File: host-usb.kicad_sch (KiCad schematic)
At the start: 15 parts, among them J3 USB4105-GF-A-060, U2 USBLC6-2SC6, U5 AP62301WU-7

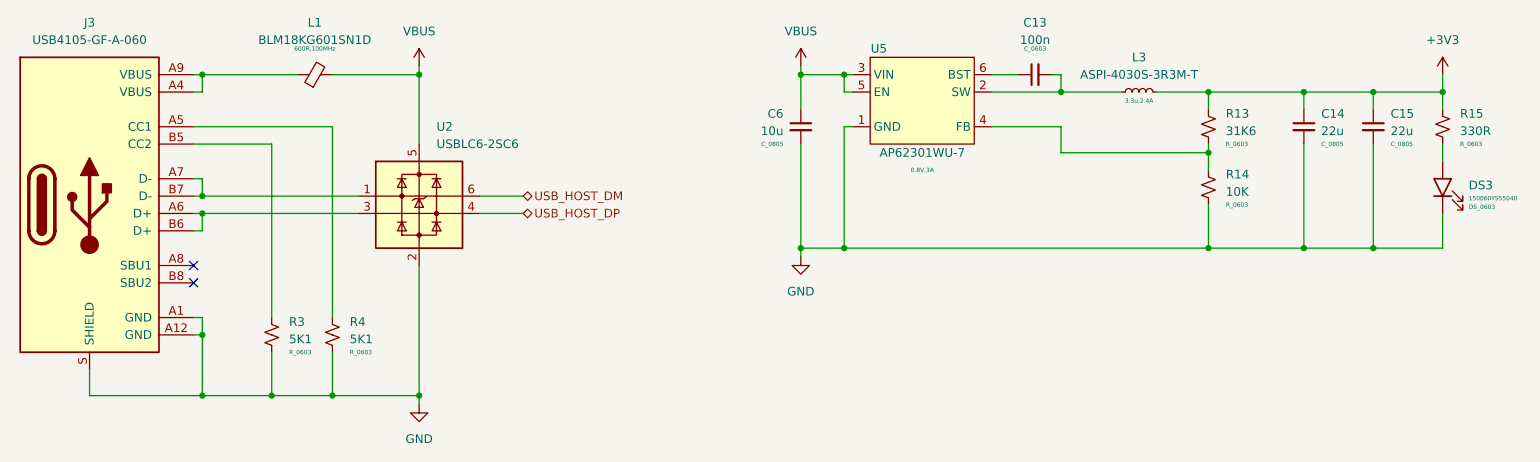
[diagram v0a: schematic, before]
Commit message: Reannotate components
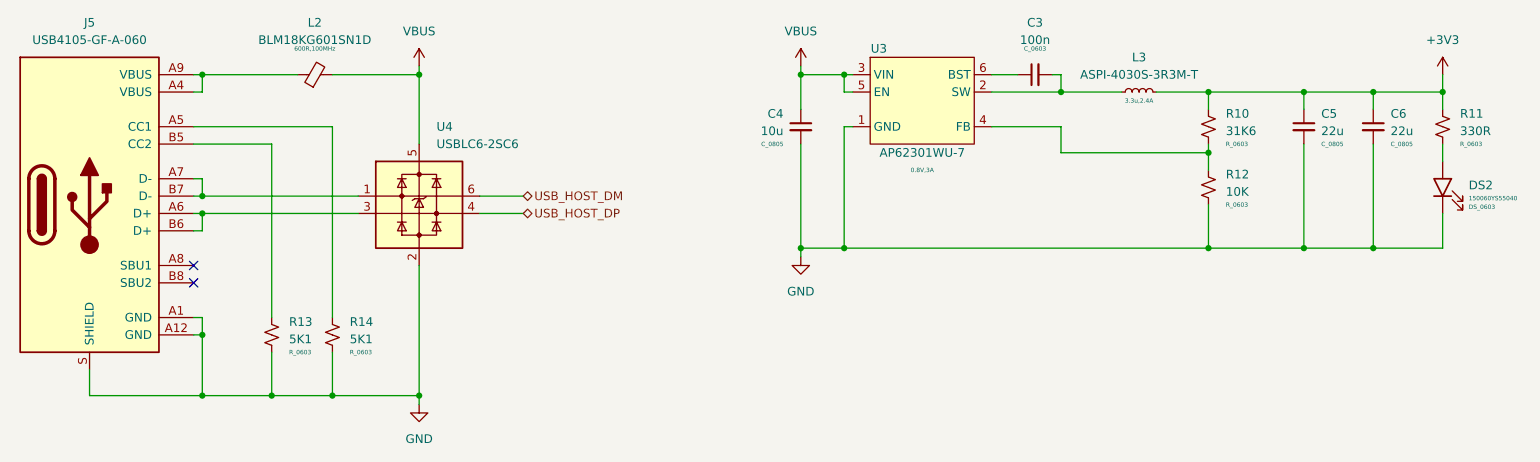
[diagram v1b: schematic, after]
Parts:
- renumbered C13 to C3, C6 to C4, C14 to C5, C15 to C6, DS3 to DS2, J3 to J5, L1 to L2, R13 to R10, R15 to R11, R14 to R12, R3 to R13, R4 to R14, U5 to U3, U2 to U4
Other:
- company: (none) -> TL Embedded
- title: (none) -> Winglet Carrier Board
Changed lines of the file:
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@@
 	(generator_version "8.0")
 	(paper "A4")
+	(title_block
+		(title "Winglet Carrier Board")
+		(date "2024-08-09")
+		(rev "v1.0")
+		(company "TL Embedded")
+	)
 	(junction
 		(at 52.07 83.82)
@@
 		(dnp no)
 		(fields_autoplaced yes)
-		(property "Reference" "C13"
+		(property "Reference" "C3"
 			(at 173.9963 58.42 90)
 			(effects
@@
 			(project ""
 				(path "/bbb905ef-a222-43ea-83e2-d1132f7d94bb/c327a527-aa7b-45f5-99fd-8bd1b67a4d25"
-					(reference "C13")
+					(reference "C3")
 					(unit 1)
 				)
@@
 		(on_board yes)
 		(dnp no)
-		(property "Reference" "C6"
+		(property "Reference" "C4"
 			(at 137.16 71.7612 0)
 			(effects
@@
 			(project ""
 				(path "/bbb905ef-a222-43ea-83e2-d1132f7d94bb/c327a527-aa7b-45f5-99fd-8bd1b67a4d25"
-					(reference "C6")
+					(reference "C4")
 					(unit 1)
 				)
@@
 		(dnp no)
 		(fields_autoplaced yes)
-		(property "Reference" "J3"
+		(property "Reference" "J5"
 			(at 35.56 58.42 0)
 			(effects
@@
 			(project "Winglet-Carrier"
 				(path "/bbb905ef-a222-43ea-83e2-d1132f7d94bb/c327a527-aa7b-45f5-99fd-8bd1b67a4d25"
-					(reference "J3")
+					(reference "J5")
 					(unit 1)
 				)
@@
 		(dnp no)
 		(fields_autoplaced yes)
-		(property "Reference" "L1"
+		(property "Reference" "L2"
 			(at 68.5419 58.42 90)
 			(effects
@@
 			(project "Winglet-Carrier"
 				(path "/bbb905ef-a222-43ea-83e2-d1132f7d94bb/c327a527-aa7b-45f5-99fd-8bd1b67a4d25"
-					(reference "L1")
+					(reference "L2")
 					(unit 1)
 				)
@@
 		(on_board yes)
 		(dnp no)
-		(property "Reference" "C15"
+		(property "Reference" "C6"
 			(at 226.06 71.7612 0)
 			(effects
@@
 			(project "Winglet-Carrier"
 				(path "/bbb905ef-a222-43ea-83e2-d1132f7d94bb/c327a527-aa7b-45f5-99fd-8bd1b67a4d25"
-					(reference "C15")
+					(reference "C6")
 					(unit 1)
 				)
@@
 		(dnp no)
 		(fields_autoplaced yes)
-		(property "Reference" "#PWR09"
+		(property "Reference" "#PWR014"
 			(at 83.82 120.65 0)
 			(effects
@@
 			(project "Winglet-Carrier"
 				(path "/bbb905ef-a222-43ea-83e2-d1132f7d94bb/c327a527-aa7b-45f5-99fd-8bd1b67a4d25"
-					(reference "#PWR09")
+					(reference "#PWR014")
 					(unit 1)
 				)
@@
 		(on_board yes)
 		(dnp no)
-		(property "Reference" "U2"
+		(property "Reference" "U4"
 			(at 86.36 73.66 0)
 			(effects
@@
 			(project "Winglet-Carrier"
 				(path "/bbb905ef-a222-43ea-83e2-d1132f7d94bb/c327a527-aa7b-45f5-99fd-8bd1b67a4d25"
-					(reference "U2")
+					(reference "U4")
 					(unit 1)
 				)
@@
 		(dnp no)
 		(fields_autoplaced yes)
-		(property "Reference" "DS3"
+		(property "Reference" "DS2"
 			(at 237.49 82.2324 90)
 			(effects
@@
 			(project ""
 				(path "/bbb905ef-a222-43ea-83e2-d1132f7d94bb/c327a527-aa7b-45f5-99fd-8bd1b67a4d25"
-					(reference "DS3")
+					(reference "DS2")
 					(unit 1)
 				)
@@
 		(on_board yes)
 		(dnp no)
-		(property "Reference" "R4"
+		(property "Reference" "R14"
 			(at 73.66 102.235 0)
 			(effects
@@
 			(project "Winglet-Carrier"
 				(path "/bbb905ef-a222-43ea-83e2-d1132f7d94bb/c327a527-aa7b-45f5-99fd-8bd1b67a4d25"
-					(reference "R4")
+					(reference "R14")
 					(unit 1)
 				)
@@
 		(dnp no)
 		(fields_autoplaced yes)
-		(property "Reference" "R13"
+		(property "Reference" "R10"
 			(at 201.93 71.7549 0)
 			(effects
@@
 			(project ""
 				(path "/bbb905ef-a222-43ea-83e2-d1132f7d94bb/c327a527-aa7b-45f5-99fd-8bd1b67a4d25"
-					(reference "R13")
+					(reference "R10")
 					(unit 1)
 				)
@@
 		(dnp no)
 		(fields_autoplaced yes)
-		(property "Reference" "R15"
+		(property "Reference" "R11"
 			(at 236.22 71.7549 0)
 			(effects
@@
 			(project "Winglet-Carrier"
 				(path "/bbb905ef-a222-43ea-83e2-d1132f7d94bb/c327a527-aa7b-45f5-99fd-8bd1b67a4d25"
-					(reference "R15")
+					(reference "R11")
 					(unit 1)
 				)
@@
 		(dnp no)
 		(fields_autoplaced yes)
-		(property "Reference" "#PWR01"
+		(property "Reference" "#PWR011"
 			(at 139.7 68.58 0)
 			(effects
@@
 			(project "Winglet-Carrier"
 				(path "/bbb905ef-a222-43ea-83e2-d1132f7d94bb/c327a527-aa7b-45f5-99fd-8bd1b67a4d25"
-					(reference "#PWR01")
+					(reference "#PWR011")
 					(unit 1)
 				)
@@
 		(dnp no)
 		(fields_autoplaced yes)
-		(property "Reference" "#PWR031"
+		(property "Reference" "#PWR012"
 			(at 233.68 69.85 0)
 			(effects
@@
 			(project ""
 				(path "/bbb905ef-a222-43ea-83e2-d1132f7d94bb/c327a527-aa7b-45f5-99fd-8bd1b67a4d25"
-					(reference "#PWR031")
+					(reference "#PWR012")
 					(unit 1)
 				)
@@
 		(on_board yes)
 		(dnp no)
-		(property "Reference" "U5"
+		(property "Reference" "U3"
 			(at 151.13 62.23 0)
 			(effects
@@
 			(project ""
 				(path "/bbb905ef-a222-43ea-83e2-d1132f7d94bb/c327a527-aa7b-45f5-99fd-8bd1b67a4d25"
-					(reference "U5")
+					(reference "U3")
 					(unit 1)
 				)
@@
 		(on_board yes)
 		(dnp no)
-		(property "Reference" "C14"
+		(property "Reference" "C5"
 			(at 215.9 71.7612 0)
 			(effects
@@
 			(project "Winglet-Carrier"
 				(path "/bbb905ef-a222-43ea-83e2-d1132f7d94bb/c327a527-aa7b-45f5-99fd-8bd1b67a4d25"
-					(reference "C14")
+					(reference "C5")
 					(unit 1)
 				)
@@
 		(dnp no)
 		(fields_autoplaced yes)
-		(property "Reference" "#PWR02"
+		(property "Reference" "#PWR013"
 			(at 139.7 99.06 0)
 			(effects
@@
 			(project "Winglet-Carrier"
 				(path "/bbb905ef-a222-43ea-83e2-d1132f7d94bb/c327a527-aa7b-45f5-99fd-8bd1b67a4d25"
-					(reference "#PWR02")
+					(reference "#PWR013")
 					(unit 1)
 				)
@@
 		(dnp no)
 		(fields_autoplaced yes)
-		(property "Reference" "R14"
+		(property "Reference" "R12"
 			(at 201.93 80.6449 0)
 			(effects
@@
 			(project "Winglet-Carrier"
 				(path "/bbb905ef-a222-43ea-83e2-d1132f7d94bb/c327a527-aa7b-45f5-99fd-8bd1b67a4d25"
-					(reference "R14")
+					(reference "R12")
 					(unit 1)
 				)
@@
 		(dnp no)
 		(fields_autoplaced yes)
-		(property "Reference" "R3"
+		(property "Reference" "R13"
 			(at 64.77 102.235 0)
 			(effects
@@
 			(project "Winglet-Carrier"
 				(path "/bbb905ef-a222-43ea-83e2-d1132f7d94bb/c327a527-aa7b-45f5-99fd-8bd1b67a4d25"
-					(reference "R3")
+					(reference "R13")
 					(unit 1)
 				)
